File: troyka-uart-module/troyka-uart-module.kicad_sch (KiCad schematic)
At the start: 2 parts, among them J1 UP (A), J2 DOWN (A)

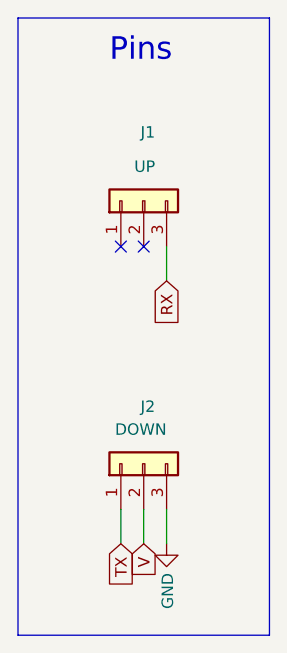
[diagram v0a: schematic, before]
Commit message: Update templates and CI
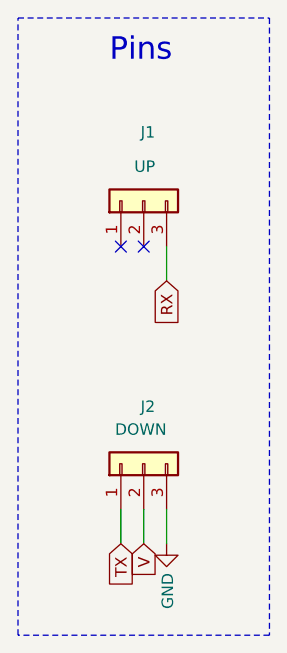
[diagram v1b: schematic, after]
